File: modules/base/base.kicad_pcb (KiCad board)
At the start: 2 copper layers, 223.5 x 160 mm, 163 parts, among them J1 LineOut, J10 Conn_01x02, J11 Conn_01x02, J12 Conn_01x02, J13 Conn_01x02, J14 Conn_01x02, J15 Conn_01x02, J16 Conn_01x02, J17 Conn_01x02, J18 Conn_01x02, J2 Ground, J4 Ground, J5 USB_C_Receptacle_PowerOnly_6P, J6 HeadphoneOut, J7 Conn_01x02, J8 Conn_01x02, J9 Conn_01x02, SW1 K2-1808SN-A4SW-01, U10 TPS2111APWR, U11 TPS2111APWR, U12 TPS2111APWR, U13 TPS2111APWR, U14 TPS2111APWR, U15 TPS2111APWR, U16 TPS2111APWR, U17 TPS2111APWR, U2 MCP6002-xSN, U3 MCP6002-xSN, U4 MCP6002-xSN, U5 AP2112K-3.3, U6 TPS2111APWR, U7 TPS2111APWR, U8 TPS2111APWR, U9 TPS2111APWR

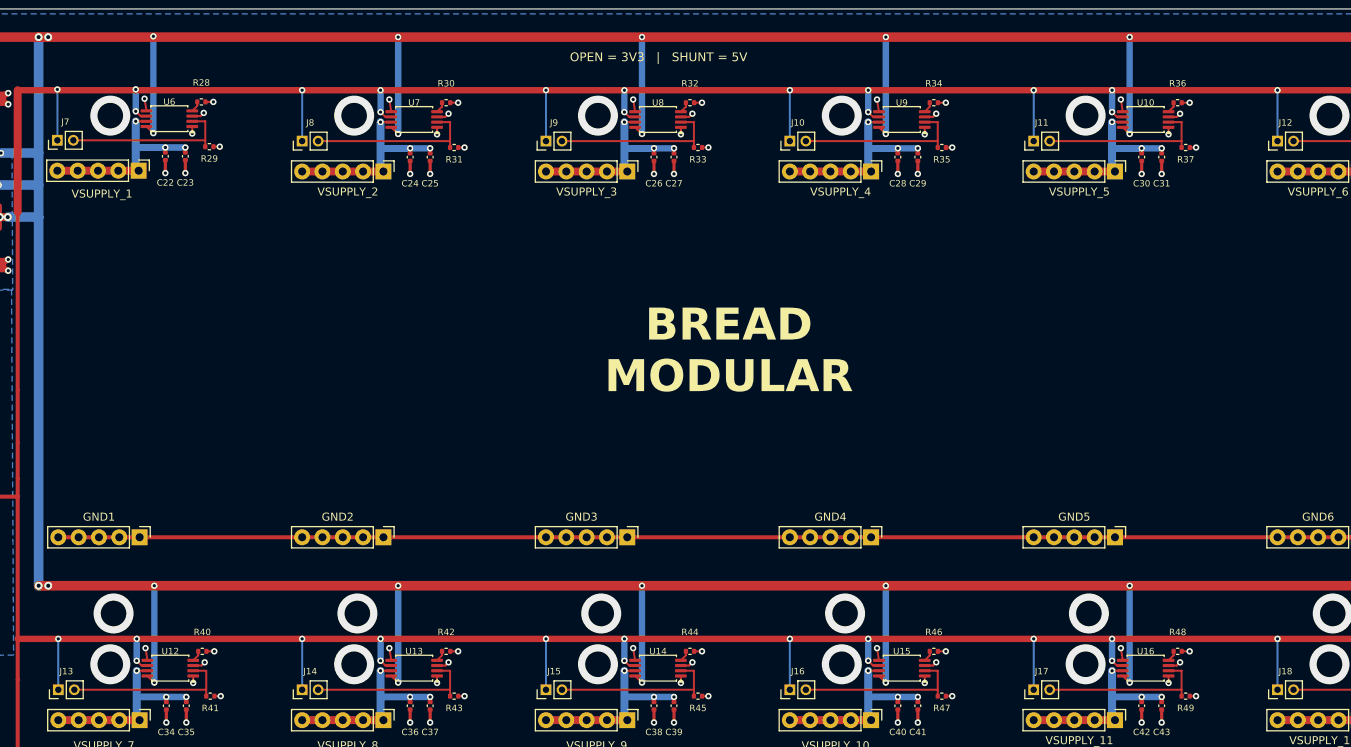
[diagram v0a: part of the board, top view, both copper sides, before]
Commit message: Add 5V indicator next to the jumper
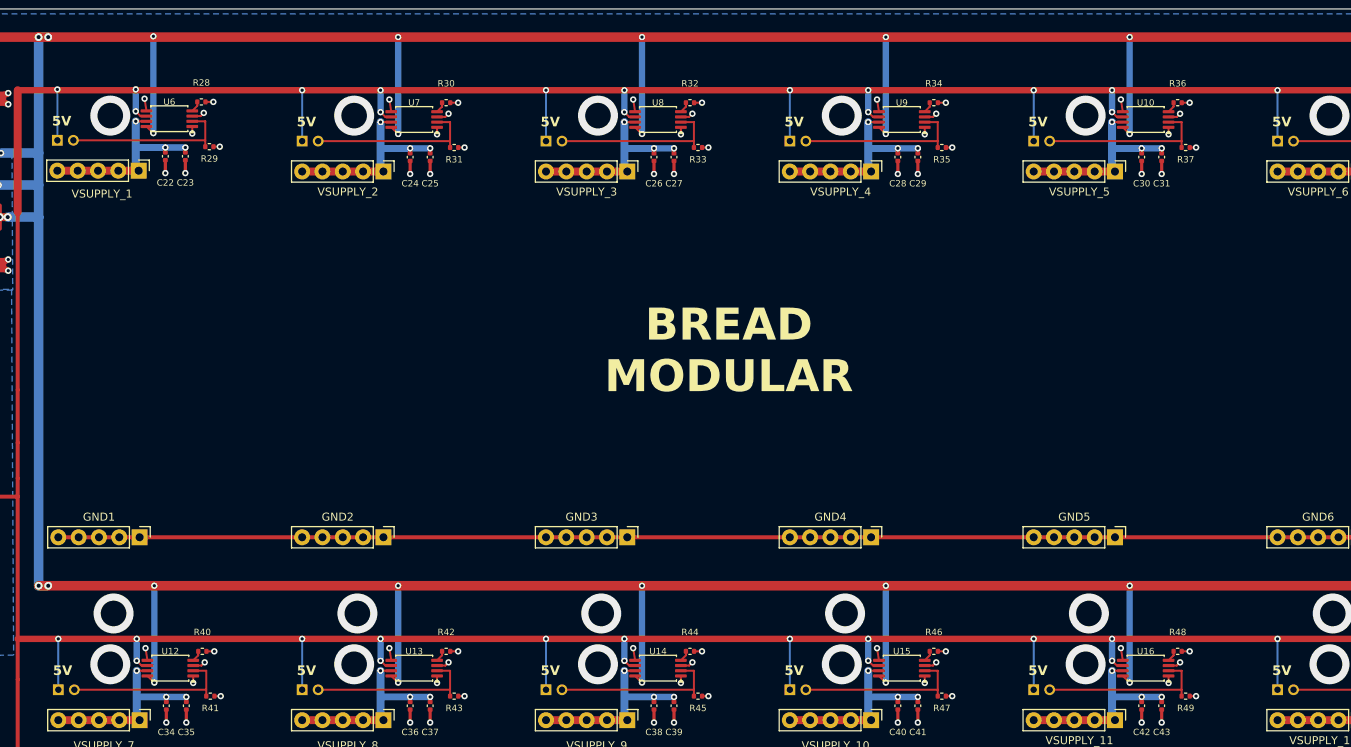
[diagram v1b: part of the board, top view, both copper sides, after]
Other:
- board text added: "5V"
- board text removed: "OPEN = 3V3 | SHUNT = 5V"

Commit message: base: line-out default gain 330k->680k for R18/R19 (+6.28 dB); record remaining loud-jumper/normalling work as pending in CHANGELOG
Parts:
- R18, R19: value 330k -> 680k
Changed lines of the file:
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@@
 			)
 		)
-		(property "Value" "330k"
+		(property "Value" "680k"
 			(at 0 1.43 0)
 			(layer "F.Fab")
@@
 			)
 		)
-		(property "Value" "330k"
+		(property "Value" "680k"
 			(at 0 1.43 180)
 			(layer "F.Fab")

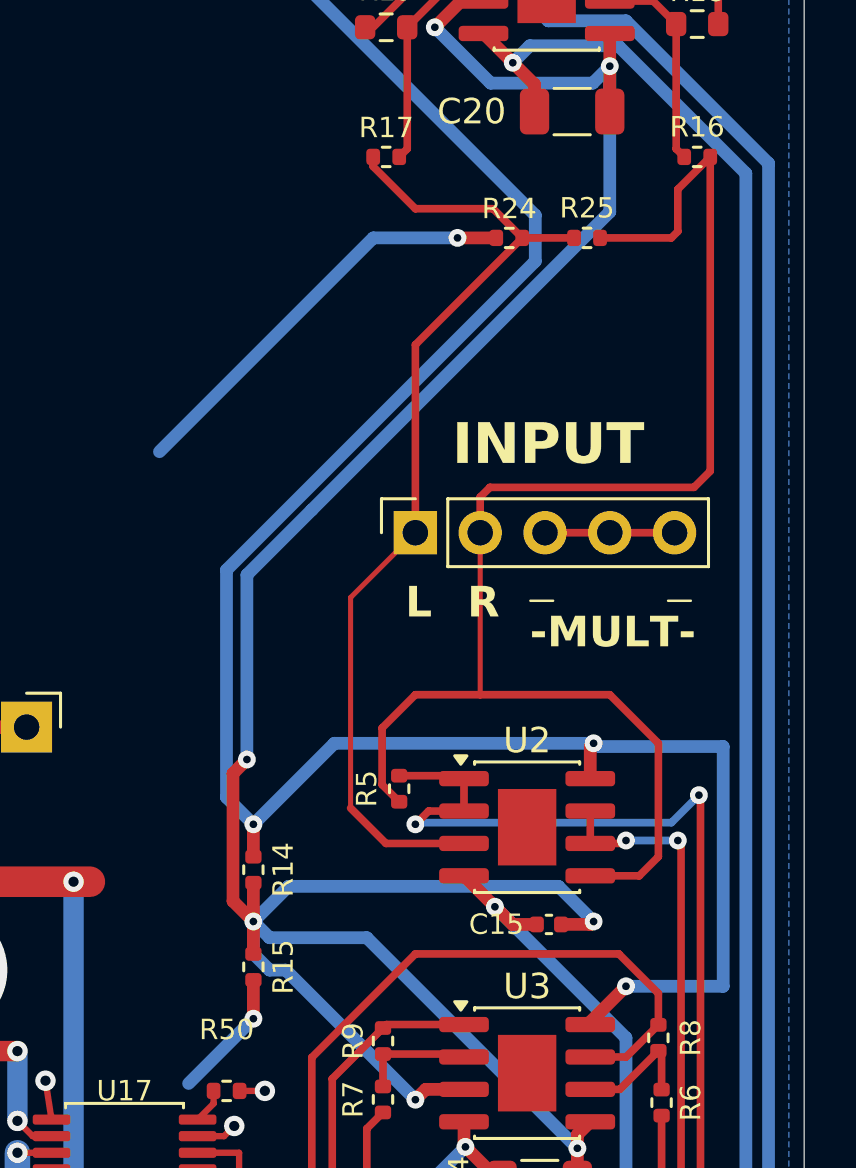
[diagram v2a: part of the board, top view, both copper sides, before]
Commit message: base: 1.3.4 - remove the leaky R25 IN_L-IN_R bridge, add the unilateral 2M R52 mono normal (J19 solder-jumper link), move R24's DC return to the 1.65V +2.5V node (R5 1M->2M); record the Phase-2 loud-gain shunt as deferred
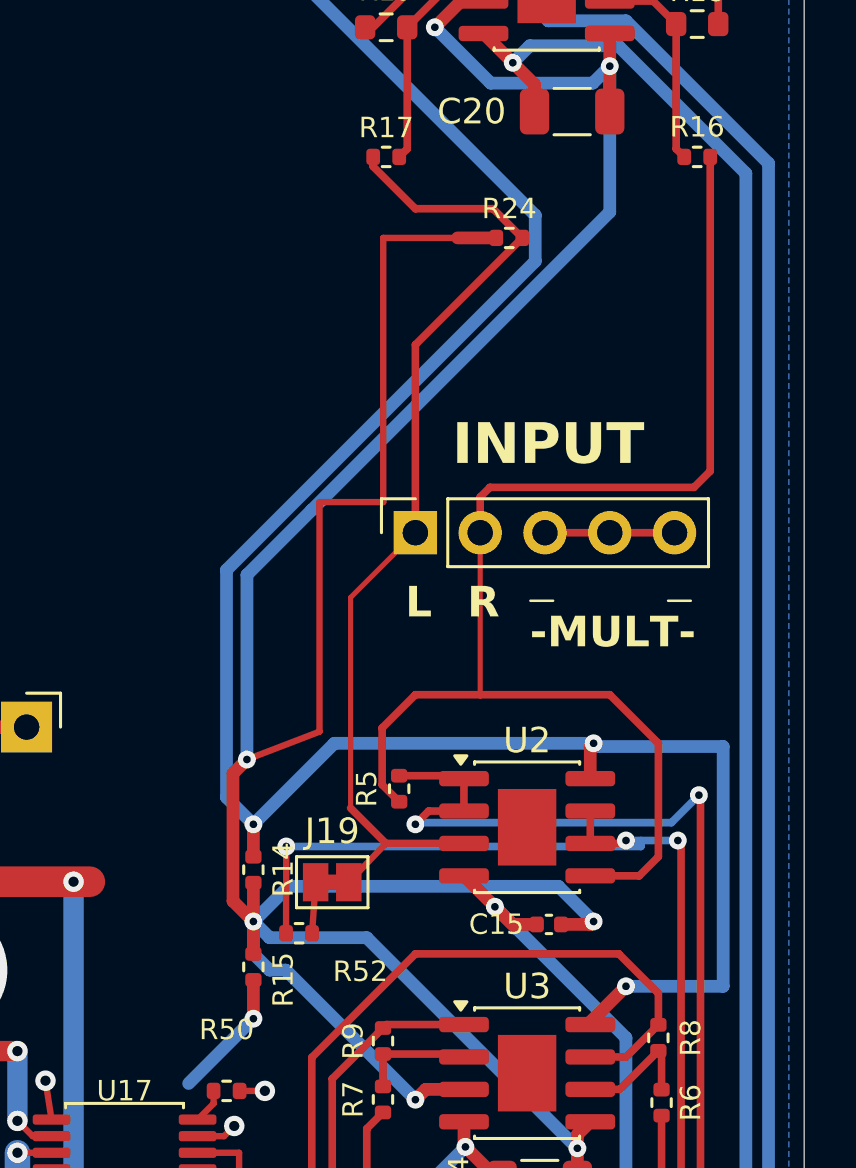
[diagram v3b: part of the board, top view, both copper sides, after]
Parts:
- removed R25: 10k, Resistor_SMD:R_0402_1005Metric
- added J19: SolderJumper_2_Bridged, Jumper:SolderJumper-2_P1.3mm_Bridged_Pad1.0x1.5mm, F.Cu at (235.5, 89.9)
- added R52: 2M, Resistor_SMD:R_0402_1005Metric, F.Cu at (234.2, 91.9)
- R24: value 10k -> 2M
- R5: value 1M -> 2M
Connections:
- R24 pad 2: GND -> +2.5V
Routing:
- net +2.5V: track 103.1 -> 130.9 mm
- net BUFF_IN_R: track 41.6 -> 59.1 mm, vias 2 -> 3
- net GND: track 1277.4 -> 1262.3 mm, vias 118 -> 117
- net IN_R: track 58.9 -> 52.3 mm
- net NORM_R: track 0.00 -> 2.00 mm

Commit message: base: 1.3.5 - line-out loud-gain option: 1M series R53/R54 + shunt solder jumper J20/J21 per channel (bridged as shipped = 680k default / +6.28 dB, cut = 1.68M / +14.14 dB vs the 330k board); schematic re-wired with the LFB_A/LFB_B and RFB_A/RFB_B nodes
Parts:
- added J20: SolderJumper_2_Bridged, Jumper:SolderJumper-2_P1.3mm_Bridged_Pad1.0x1.5mm, F.Cu at (238.4, 59.0)
- added J21: SolderJumper_2_Bridged, Jumper:SolderJumper-2_P1.3mm_Bridged_Pad1.0x1.5mm, F.Cu at (249.0, 59.0)
- added R53: 1M, Resistor_SMD:R_0402_1005Metric, F.Cu at (240.7, 59.0)
- added R54: 1M, Resistor_SMD:R_0402_1005Metric, F.Cu at (250.8, 59.0)
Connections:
- R16 pad 1: Net-(U4B--) -> RFB_B
- R17 pad 1: Net-(U4A--) -> LFB_B
- R18 pad 2: Net-(U4B--) -> RFB_A
- R19 pad 2: Net-(U4A--) -> LFB_A
- U4 pad 2: Net-(U4A--) -> LFB_A
- U4 pad 6: Net-(U4B--) -> RFB_A
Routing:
- net Net-(U4A--): track 9.15 -> 0.00 mm
- net Net-(U4B--): track 8.31 -> 0.00 mm
- net LFB_A: track 0.00 -> 8.16 mm
- net RFB_A: track 0.00 -> 6.98 mm
- net LFB_B: track 0.00 -> 4.11 mm
- net RFB_B: track 0.00 -> 3.77 mm

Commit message: base: 1.3.6 Phase A - remove the passive mono normal (R52+J19), restore the symmetric stereo input path
- delete R52 + J19 and the NORM_R net (schematic, plus the PCB copper that only fed them: the
  IN_L stub to J19.1, R52's F.Cu stub, the BUFF_IN_R B.Cu trunk+jog and the via at
  (233.700,88.500)); BUFF_IN_R keeps its U2.6/U2.7 -> RV1.3 path, nothing is left dangling
- R5 2M pin 1 moves from BUFF_IN_L to the 1.65V node +2.5V, so R5 (right) and R24 (left) are
  identical per-channel bias returns: 2M||1M = 667k input impedance and -680k/1M = -0.68 =
  -3.35 dB on both channels (0.000 dB L/R difference), no DC current in R17/R16 and both amp
  outputs at 1.65V; 2M keeps the already-sourced C11512 part and does not load the 500R bias
  source (a 2M return also does not shift the node off 1.65V)
- PCB: R5 is not moved; R5.1 -> 1 F.Cu stub -> 1 via -> 2 B.Cu segments landing on the existing
  +2.5V horizontal at y=90.062 (an all-F.Cu route is impossible: the IN_L trace walls the pocket)
- correct a latent net-code bug: the existing (241.929,64.643)-(240.411,64.643) +2.5V return
  segment was still stored as net 1 (GND); now net 18 (+2.5V). No geometry change
- verification: sch erc == baseline (11 findings, identical kinds); pcb drc --schematic-parity
  == 0 errors / 0 unconnected / 145 parity items (== baseline); 80 violations = 71
  lib_footprint_mismatch (baseline 73 minus the two removed footprints) + the baseline's 5
  silk_overlap and 4 silk_over_copper, i.e. no new item. Netlist proof: 1.3.5 has
  BUFF_IN_L -R5- IN_R and BUFF_IN_R -R52- NORM_R -J19- IN_L; this revision has no passive path
  between the left and right signal chains (supply/GND excluded)
- headphone block and the loud-gain parts byte-identical (U3, R6/R7, RV1/RV2, C3/C7-C13,
  R8/R9/R10/R12, J1, J6, C18/C19, R20/R21, R53/R54+J20/J21, R16/R17/R18/R19, U2/U4, R14/R15)
- board diff 791+/1266-: 1503 of those lines are the re-poured B.Cu GND polygon (only 1 of the
  49 filled polygons changed)
- VERSION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
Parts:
- removed J19: SolderJumper_2_Bridged, Jumper:SolderJumper-2_P1.3mm_Bridged_Pad1.0x1.5mm
- removed R52: 2M, Resistor_SMD:R_0402_1005Metric
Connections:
- R5 pad 1: BUFF_IN_L -> +2.5V
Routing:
- net BUFF_IN_R: track 59.1 -> 41.6 mm, vias 3 -> 2
- net +2.5V: track 130.9 -> 137.1 mm, vias 7 -> 8
- net BUFF_IN_L: track 74.5 -> 72.1 mm
- net IN_L: track 39.6 -> 37.5 mm
- net NORM_R: track 2.00 -> 0.00 mm
- net GND: track 1262.3 -> 1260.8 mm

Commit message: base: 1.3.6 Phase B - mono mode as a selector jumper at the right line-amp input (J22), right input discarded
- J22 = Jumper:SolderJumper-3_P1.3mm_Bridged12_Pad1.0x1.5mm at (250.317,66.5), symbol
  Connector_Generic:Conn_01x03 with Value SolderJumper_3_Bridged12 (in_bom no) and
  net_tie_pad_groups "1, 2": pad 1 = IN_R, pad 2 = RIN_SEL (new net) = R16's input pin,
  pad 3 = BUFF_IN_L
- as shipped (pads 1-2 bridged) the right line-amp input is its own channel input IN_R: pure
  stereo, no passive path between the left and right chains
- mono (cut the 1-2 bridge, bridge 2-3) drives the right line amp from the buffered LEFT signal
  while IN_R is reduced to its 2M bias return R5, so the right input reaches no line output
- level: unity-gain buffer + R16 = R17 = 1M into R18 = R19 = 680k gives -0.68 = -3.35 dB on both
  channels in both positions (0.00 dB L/R; loud state -(680k+1M)/1M = -4.51 dB on both too), so no
  series resistor is needed; DC: RIN_SEL sits at 1.65V in both positions (no DC step, no offset
  through R16)
- PCB: the old IN_R run into R16.2 is replaced by three F.Cu links (J22.2 -> R16.2; J22.1 -> IN_R,
  with the old 45-degree jog removed so nothing dangles; J22.3 -> BUFF_IN_L through x = 252.9).
  All new copper is F.Cu only, so this phase re-poured no zone
- verification: sch erc == baseline (11 findings, identical kinds); pcb drc --schematic-parity ==
  0 errors / 0 unconnected / 146 parity items (145 baseline + J22's field comparison, same class);
  81 violations = 72 lib_footprint_mismatch + the baseline's 5 silk_overlap and 4
  silk_over_copper - no new violation class, no new silkscreen item
- netlist proof: stereo = no passive path between the chains; mono = the only path is the intended
  BUFF_IN_L -J22- RIN_SEL -R16- RFB_B, with IN_R left with just its 2M bias return
- headphone block and loud-gain parts byte-identical (U3, R6/R7, RV1/RV2, C3/C7-C13, R8/R9/R10/R12,
  J1, J6, C18/C19, R20/R21, R53/R54+J20/J21): mono is confined to the line out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
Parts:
- added J22: SolderJumper_3_Bridged12, Jumper:SolderJumper-3_P1.3mm_Bridged12_Pad1.0x1.5mm, F.Cu at (250.3, 66.5)
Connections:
- R16 pad 2: IN_R -> RIN_SEL
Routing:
- net BUFF_IN_L: track 72.1 -> 94.8 mm
- net IN_R: track 52.3 -> 46.3 mm
- net RIN_SEL: track 0.00 -> 5.03 mm

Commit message: BASE 1.3.13: complete candidate and bounded post-review improvements
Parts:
- removed J20, J21: SolderJumper_2_Bridged, Jumper:SolderJumper-2_P1.3mm_Bridged_Pad1.0x1.5mm
- removed J22: SolderJumper_3_Bridged12, Jumper:SolderJumper-3_P1.3mm_Bridged12_Pad1.0x1.5mm
- removed R28, R30, R32, R34, R36, R38, R40, R42, R44, R46, R48, R50: 750, Resistor_SMD:R_0402_1005Metric
- removed R53, R54: 1M, Resistor_SMD:R_0402_1005Metric
- added C48: 100n, Capacitor_SMD:C_0402_1005Metric, F.Cu at (248.7, 65.0)
- added C50: 0.1uf, Capacitor_SMD:C_0402_1005Metric, F.Cu at (244.7, 83.7)
- added C51: 0.1uf, Capacitor_SMD:C_0402_1005Metric, F.Cu at (245.6, 93.7)
- added C52: 0.1uf, Capacitor_SMD:C_0402_1005Metric, F.Cu at (247.7, 51.4)
- added J23: PZ200-1-02-Z, Connector_PinHeader_2.00mm:PinHeader_1x02_P2.00mm_Vertical, F.Cu at (248.0, 72.4)
- added R55: 100k, Resistor_SMD:R_0402_1005Metric, F.Cu at (240.5, 69.0)
- added R57: 100, Resistor_SMD:R_0402_1005Metric, F.Cu at (246.4, 79.4)
- added R58: 10k, Resistor_SMD:R_0402_1005Metric, F.Cu at (238.8, 72.2)
- added R59: 10k, Resistor_SMD:R_0402_1005Metric, F.Cu at (241.3, 72.2)
- added U18: TS5A23157DGS, Package_SO:TSSOP-10_3x3mm_P0.5mm, F.Cu at (249.0, 68.2)
- U10, U11, U12, U13, U14, U15, U16, U17, U6, U7, U8, U9: value TPS2111APWR -> TPS2116DRLR; footprint Package_SO:TSSOP-8_4.4x3mm_P0.65mm -> Package_TO_SOT_SMD:SOT-583-8
- U2, U4: footprint Package_SO:SOIC-8-1EP_3.9x4.9mm_P1.27mm_EP2.29x3mm -> Package_SO:SOIC-8_3.9x4.9mm_P1.27mm
- U3: value MCP6002-xSN -> TS922IDT; footprint Package_SO:SOIC-8-1EP_3.9x4.9mm_P1.27mm_EP2.29x3mm -> Package_SO:SOIC-8_3.9x4.9mm_P1.27mm
- moved C23 3.28 mm to (74.8, 33.6), turned to 0 degrees
- moved C25 3.28 mm to (105.4, 33.7), turned to 0 degrees
- moved C27 3.28 mm to (135.9, 33.7), turned to 0 degrees
- moved C29 3.28 mm to (166.4, 33.7), turned to 0 degrees
- moved C31 3.28 mm to (196.9, 33.7), turned to 0 degrees
- moved C33 3.28 mm to (227.4, 33.7), turned to 0 degrees
- moved C35 3.28 mm to (75.0, 102.3), turned to 0 degrees
- moved C37 3.28 mm to (105.4, 102.3), turned to 0 degrees
- moved C39 3.28 mm to (135.9, 102.3), turned to 0 degrees
- moved C41 3.28 mm to (166.4, 102.3), turned to 0 degrees
- moved C43 3.28 mm to (196.9, 102.3), turned to 0 degrees
- moved C45 3.28 mm to (227.4, 102.3), turned to 0 degrees
- moved C22 1.30 mm to (74.8, 35.0), turned to 0 degrees
- moved C24 1.30 mm to (105.4, 35.1), turned to 0 degrees
- moved C26 1.30 mm to (135.9, 35.1), turned to 0 degrees
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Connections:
- J10 pad 1: +3.3V -> VBUS_PROT
- J11 pad 1: +3.3V -> VBUS_PROT
- J12 pad 1: +3.3V -> VBUS_PROT
- J13 pad 1: +3.3V -> VBUS_PROT
- J14 pad 1: +3.3V -> VBUS_PROT
- J15 pad 1: +3.3V -> VBUS_PROT
- J16 pad 1: +3.3V -> VBUS_PROT
- J17 pad 1: +3.3V -> VBUS_PROT
- J18 pad 1: +3.3V -> VBUS_PROT
- J7 pad 1: +3.3V -> VBUS_PROT
- J8 pad 1: +3.3V -> VBUS_PROT
- J9 pad 1: +3.3V -> VBUS_PROT
- R16 pad 1: RFB_B -> RFB_A
- R17 pad 1: LFB_B -> LFB_A
- R17 pad 2: IN_L -> IN_L_PROT
- R24 pad 1: IN_L -> IN_L_PROT
- R5 pad 2: IN_R -> IN_R_PROT
- U10 pad 2: SEL_5 -> VSLOT_5
- U10 pad 3: GND -> 5V_SYS
- U10 pad 4: Net-(U10-ILIM) -> SEL_5
- U10 pad 5: GND -> VBUS_PROT
- U10 pad 8: 5V_SYS -> unconnected-(U10-ST-Pad8)
- U11 pad 2: SEL_6 -> VSLOT_6
- U11 pad 3: GND -> 5V_SYS
- U11 pad 4: Net-(U11-ILIM) -> SEL_6
- U11 pad 5: GND -> VBUS_PROT
- U11 pad 8: 5V_SYS -> unconnected-(U11-ST-Pad8)
- U12 pad 2: SEL_7 -> VSLOT_7
- U12 pad 3: GND -> 5V_SYS
- U12 pad 4: Net-(U12-ILIM) -> SEL_7
- U12 pad 5: GND -> VBUS_PROT
- U12 pad 8: 5V_SYS -> unconnected-(U12-ST-Pad8)
- U13 pad 2: SEL_8 -> VSLOT_8
- U13 pad 3: GND -> 5V_SYS
- U13 pad 4: Net-(U13-ILIM) -> SEL_8
- U13 pad 5: GND -> VBUS_PROT
- U13 pad 8: 5V_SYS -> unconnected-(U13-ST-Pad8)
- U14 pad 2: SEL_9 -> VSLOT_9
- U14 pad 3: GND -> 5V_SYS
- U14 pad 4: Net-(U14-ILIM) -> SEL_9
- U14 pad 5: GND -> VBUS_PROT
- U14 pad 8: 5V_SYS -> unconnected-(U14-ST-Pad8)
- U15 pad 2: SEL_10 -> VSLOT_10
- U15 pad 3: GND -> 5V_SYS
- U15 pad 4: Net-(U15-ILIM) -> SEL_10
- U15 pad 5: GND -> VBUS_PROT
- U15 pad 8: 5V_SYS -> unconnected-(U15-ST-Pad8)
- U16 pad 2: SEL_11 -> VSLOT_11
- U16 pad 3: GND -> 5V_SYS
- U16 pad 4: Net-(U16-ILIM) -> SEL_11
- U16 pad 5: GND -> VBUS_PROT
- U16 pad 8: 5V_SYS -> unconnected-(U16-ST-Pad8)
- U17 pad 2: SEL_12 -> VSLOT_12
- U17 pad 3: GND -> 5V_SYS
- U17 pad 4: Net-(U17-ILIM) -> SEL_12
- U17 pad 5: GND -> VBUS_PROT
- U17 pad 8: 5V_SYS -> unconnected-(U17-ST-Pad8)
- U2 pad 3: IN_L -> IN_L_PROT
- U2 pad 5: IN_R -> IN_R_PROT
- U6 pad 2: SEL_1 -> VSLOT_1
- U6 pad 3: GND -> 5V_SYS
- U6 pad 4: Net-(U6-ILIM) -> SEL_1
- U6 pad 5: GND -> VBUS_PROT
- U6 pad 8: 5V_SYS -> unconnected-(U6-ST-Pad8)
- U7 pad 2: SEL_2 -> VSLOT_2
- U7 pad 3: GND -> 5V_SYS
- U7 pad 4: Net-(U7-ILIM) -> SEL_2
- U7 pad 5: GND -> VBUS_PROT
- U7 pad 8: 5V_SYS -> unconnected-(U7-ST-Pad8)
- U8 pad 2: SEL_3 -> VSLOT_3
- U8 pad 3: GND -> 5V_SYS
- U8 pad 4: Net-(U8-ILIM) -> SEL_3
- U8 pad 5: GND -> VBUS_PROT
- U8 pad 8: 5V_SYS -> unconnected-(U8-ST-Pad8)
- U9 pad 2: SEL_4 -> VSLOT_4
- U9 pad 3: GND -> 5V_SYS
- U9 pad 4: Net-(U9-ILIM) -> SEL_4
- U9 pad 5: GND -> VBUS_PROT
- U9 pad 8: 5V_SYS -> unconnected-(U9-ST-Pad8)
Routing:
- net VBUS_PROT: track 35.3 -> 711.5 mm, vias 0 -> 41
- net GND: track 1260.8 -> 1071.9 mm, vias 117 -> 89
- net IN_R_PROT: track 0.00 -> 43.3 mm
- net IN_R: track 46.3 -> 3.49 mm
- net IN_L_PROT: track 0.00 -> 39.0 mm
- net IN_L: track 37.5 -> 3.49 mm
- net MONO_SEL: track 0.00 -> 32.5 mm, vias 0 -> 3
- net +3.3V: track 772.1 -> 744.8 mm, vias 41 -> 32
- net 5V_SYS: track 602.5 -> 623.0 mm
- net RIN_SEL: track 5.03 -> 13.4 mm, vias 0 -> 2
- net SEL_1: track 21.3 -> 26.5 mm
- net SEL_6: track 21.3 -> 26.5 mm
- net SEL_5: track 21.3 -> 26.5 mm
- net SEL_4: track 21.3 -> 26.5 mm
- net SEL_3: track 21.3 -> 26.5 mm
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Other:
- board text added: "BASE 1.3.13"
- board text added: "J23 LINE MONO"
- board text added: "OPEN=STEREO"
- board text added: "RETURN 100R"
- board text removed: "-MULT-"
- board text removed: "BASE 1.3.0"
